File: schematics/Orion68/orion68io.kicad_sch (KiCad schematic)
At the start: 38 parts, among them J1 LevelConverter, J200 Euro96pin, U200 GAL16V8, U25 SN74LVC245APW, U26 SN74LVC245APW, U27 RP5C01A, U30 LM2937xT, Y3 Crystal

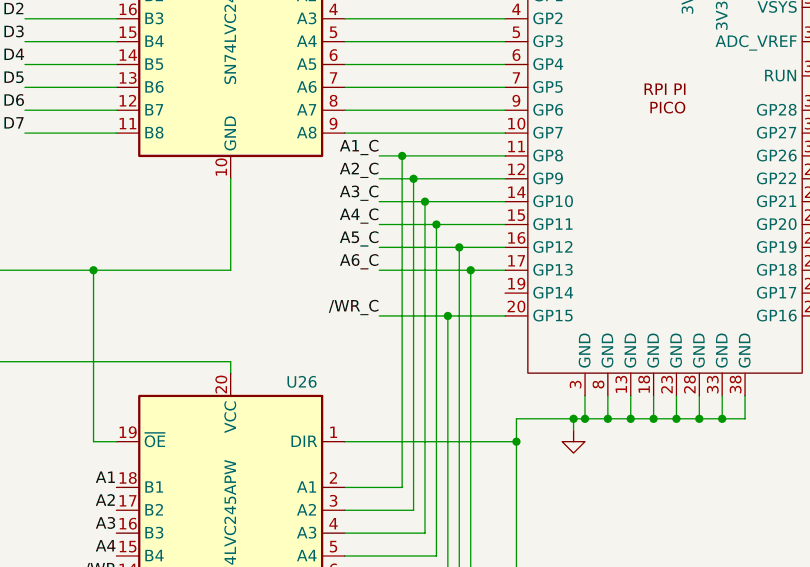
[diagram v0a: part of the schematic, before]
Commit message: Implemented CS_KBD
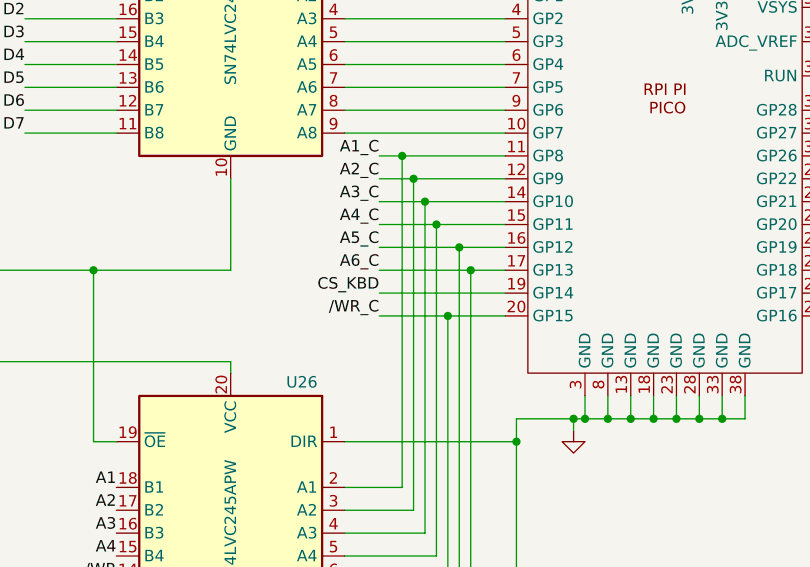
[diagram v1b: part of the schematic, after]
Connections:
- net CS_KBD: now also U_S200.19 (GP14)
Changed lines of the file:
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@@
 	(wire
 		(pts
+			(xy 176.53 143.51) (xy 190.5 143.51)
+		)
+		(stroke
+			(width 0)
+			(type default)
+		)
+	)
+	(wire
+		(pts
 			(xy 176.53 133.35) (xy 181.61 133.35)
 		)
@@
 		)
 	)
+	(label "CS_KBD"
+		(at 176.53 143.51 180)
+		(effects
+			(font
+				(size 1.27 1.27)
+			)
+			(justify right bottom)
+		)
+	)

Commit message: Changed dtack system
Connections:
- net RX_OUT is gone; now on net CS_KBD: J1.9 (Pin_9)
- net CS_KBD: no longer U_S200.19 (GP14)
- net /CS_MULTIO: now also J200.60
- net /DTACK_MIO: now reaches J200.61
- net /DTACK_MIO: now also U_S200.19 (GP14)
- net RX renamed CS_KBD_C
- net TX: no longer names the net of J1.4 (Pin_4)
- net TX_OUT: no longer names the net of J1.3 (Pin_3)
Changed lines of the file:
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@@
 	(wire
 		(pts
+			(xy -26.67 137.16) (xy -26.67 114.3)
+		)
+		(stroke
+			(width 0)
+			(type default)
+		)
+	)
+	(wire
+		(pts
 			(xy 270.51 207.01) (xy 270.51 208.28)
 		)
@@
 	(wire
 		(pts
+			(xy -26.67 114.3) (xy -24.13 114.3)
+		)
+		(stroke
+			(width 0)
+			(type default)
+		)
+	)
+	(wire
+		(pts
 			(xy -10.16 116.84) (xy -13.97 116.84)
 		)
@@
 	(wire
 		(pts
+			(xy -29.21 134.62) (xy -29.21 116.84)
+		)
+		(stroke
+			(width 0)
+			(type default)
+		)
+	)
+	(wire
+		(pts
 			(xy -12.7 50.8) (xy -13.97 50.8)
 		)
@@
 	(wire
 		(pts
+			(xy -31.75 137.16) (xy -26.67 137.16)
+		)
+		(stroke
+			(width 0)
+			(type default)
+		)
+	)
+	(wire
+		(pts
 			(xy -34.29 119.38) (xy -35.56 119.38)
 		)
@@
 	(wire
 		(pts
+			(xy -29.21 116.84) (xy -24.13 116.84)
+		)
+		(stroke
+			(width 0)
+			(type default)
+		)
+	)
+	(wire
+		(pts
 			(xy 172.72 113.03) (xy 190.5 113.03)
 		)
@@
 	(wire
 		(pts
+			(xy -31.75 134.62) (xy -29.21 134.62)
+		)
+		(stroke
+			(width 0)
+			(type default)
+		)
+	)
+	(wire
+		(pts
 			(xy 232.41 248.92) (xy 242.57 248.92)
 		)
@@
 		)
 	)
-	(label "TX_OUT"
-		(at 276.86 125.73 0)
-		(effects
-			(font
-				(size 1.27 1.27)
-			)
-			(justify left bottom)
-		)
-	)
 	(label "D3"
 		(at -34.29 55.88 0)
@@
 		)
 	)
-	(label "RX"
-		(at 264.16 133.35 180)
-		(effects
-			(font
-				(size 1.27 1.27)
-			)
-			(justify right bottom)
-		)
-	)
 	(label "5V"
 		(at 276.86 130.81 0)
@@
 		)
 	)
+	(label "CS_KBD"
+		(at 276.86 133.35 0)
+		(effects
+			(font
+				(size 1.27 1.27)
+			)
+			(justify left bottom)
+		)
+	)
 	(label "{slash}iowr"
 		(at -12.7 71.12 0)
@@
 		)
 	)
+	(label "{slash}CS_MULTIO"
+		(at -31.75 137.16 180)
+		(effects
+			(font
+				(size 1.27 1.27)
+			)
+			(justify right bottom)
+		)
+	)
 	(label "A4"
 		(at 147.32 172.72 180)
@@
 		)
 	)
+	(label "{slash}DTACK_MIO"
+		(at -31.75 134.62 180)
+		(effects
+			(font
+				(size 1.27 1.27)
+			)
+			(justify right bottom)
+		)
+	)
 	(label "+12V"
 		(at -6.35 121.92 0)
@@
 		)
 	)
-	(label "RX_OUT"
-		(at 276.86 133.35 0)
-		(effects
-			(font
-				(size 1.27 1.27)
-			)
-			(justify left bottom)
-		)
-	)
 	(label "D1"
 		(at 137.16 110.49 180)
@@
 		)
 	)
-	(label "CS_KBD"
+	(label "{slash}DTACK_MIO"
 		(at 176.53 143.51 180)
 		(effects
@@
 		)
 	)
-	(label "TX"
-		(at 264.16 125.73 180)
-		(effects
-			(font
-				(size 1.27 1.27)
-			)
-			(justify right bottom)
-		)
-	)
 	(label "A5"
 		(at -34.29 101.6 0)
@@
 		)
 	)
+	(label "CS_KBD_C"
+		(at 264.16 133.35 180)
+		(effects
+			(font
+				(size 1.27 1.27)
+			)
+			(justify right bottom)
+		)
+	)

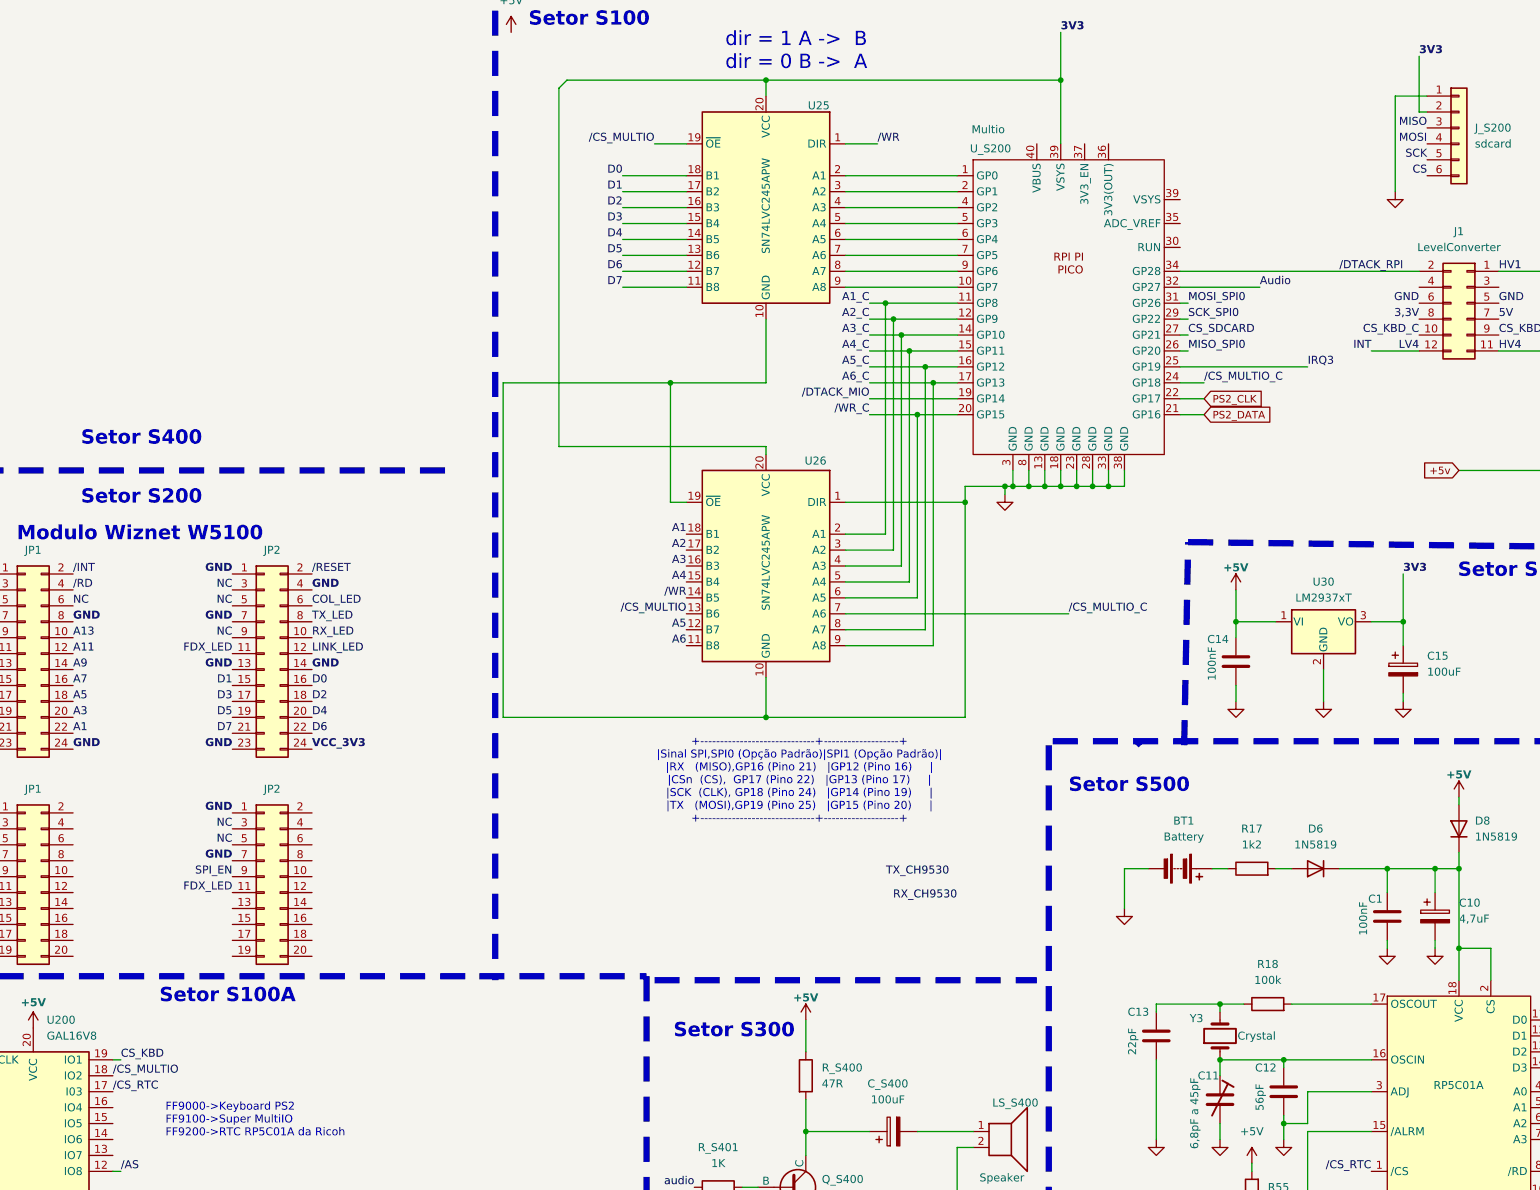
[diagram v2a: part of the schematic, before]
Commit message: SDcard running ok with pico MultiIO
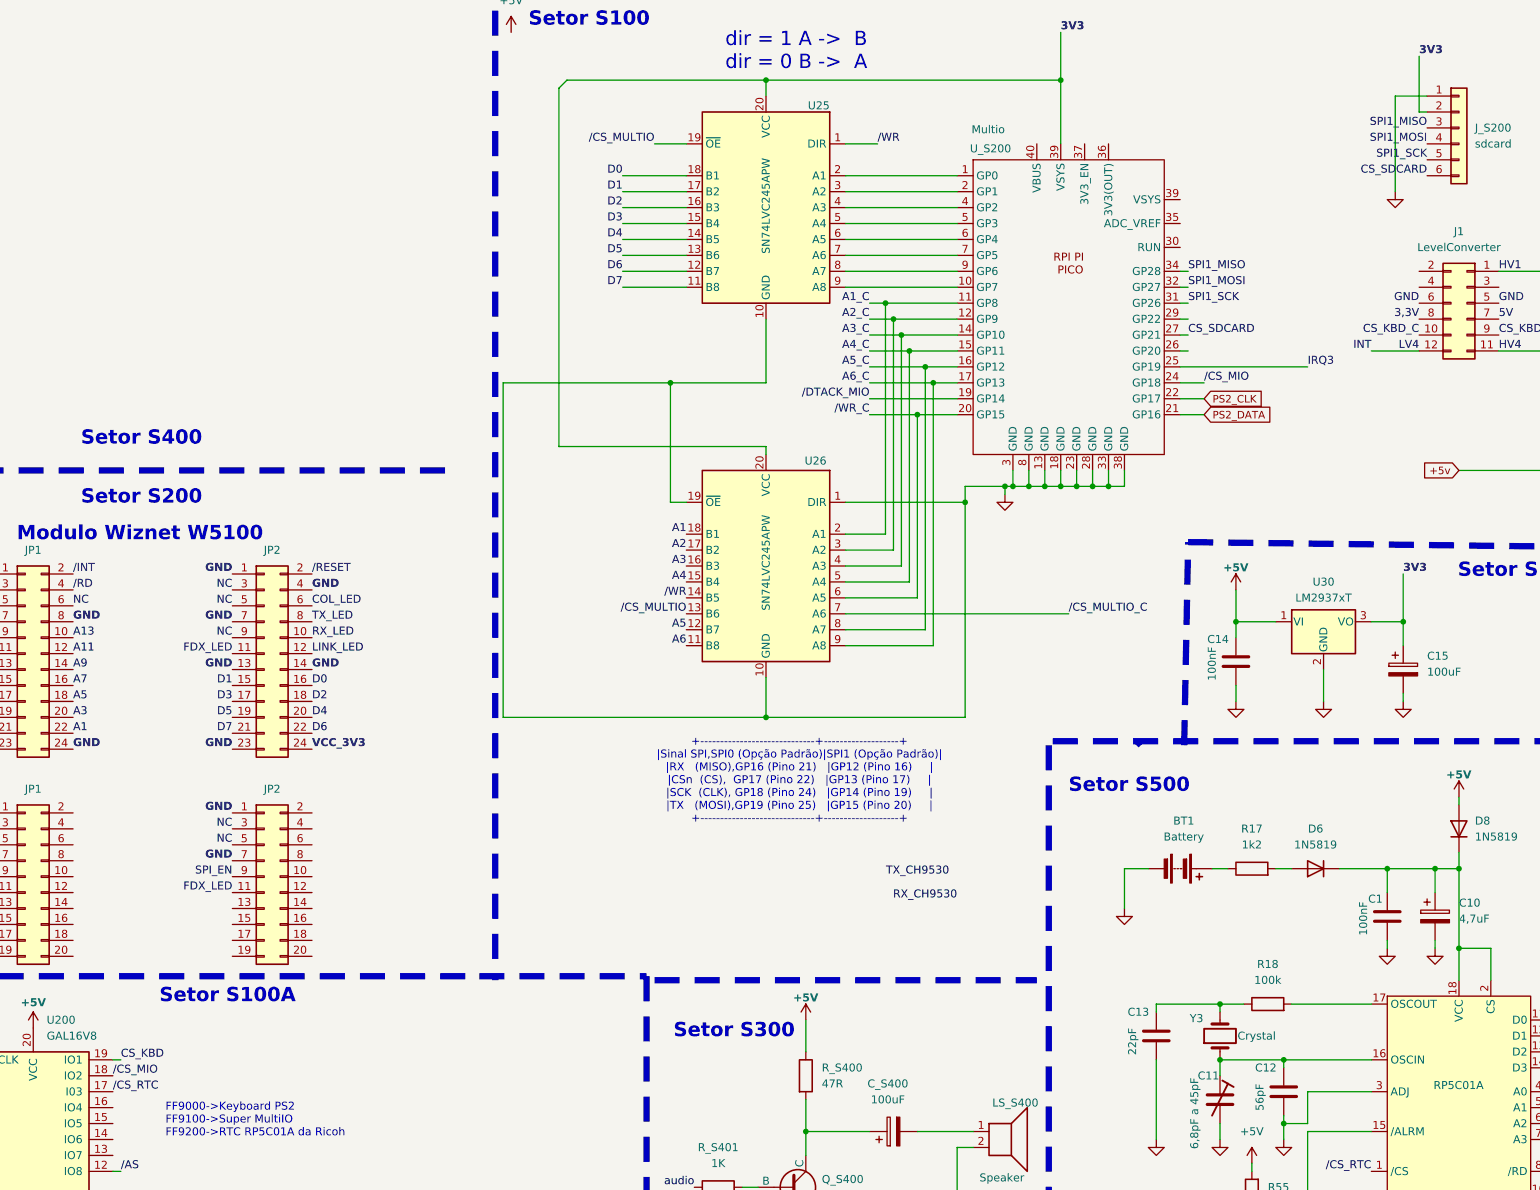
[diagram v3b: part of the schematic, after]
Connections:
- net CS is gone; now on net CS_SDCARD: J_S200.6 (Pin_6)
- net MOSI is gone; now on net SPI1_MOSI: J_S200.4 (Pin_4)
- net SCK is gone; now on net SPI1_SCK: J_S200.5 (Pin_5)
- net /CS_MULTIO: no longer U200.18 (IO2)
- net /CS_MULTIO_C: no longer U_S200.24 (GP18)
- net Audio renamed SPI1_MOSI
- net MISO renamed SPI1_MISO
- net SPI1_MISO: now also U_S200.34 (GP28)
- net MISO_SPI0: no longer names the net of U_S200.26 (GP20)
- net MOSI_SPI0 renamed SPI1_SCK
- net SCK_SPI0: no longer names the net of U_S200.29 (GP22)
- net /DTACK_RPI: no longer names the net of J1.2 (Pin_2)
- net /DTACK_RPI: no longer U_S200.34 (GP28)
- new net /CS_MIO: U200.18 (IO2), U_S200.24 (GP18)
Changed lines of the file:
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@@
 	(wire
 		(pts
+			(xy 227.33 123.19) (xy 226.06 123.19)
+		)
+		(stroke
+			(width 0)
+			(type default)
+		)
+	)
+	(wire
+		(pts
 			(xy 232.41 261.62) (xy 232.41 259.08)
 		)
@@
 	(wire
 		(pts
-			(xy 226.06 123.19) (xy 264.16 123.19)
-		)
-		(stroke
-			(width 0)
-			(type default)
-		)
-	)
-	(wire
-		(pts
 			(xy -29.21 134.62) (xy -29.21 116.84)
 		)
@@
 	(wire
 		(pts
+			(xy 227.33 125.73) (xy 226.06 125.73)
+		)
+		(stroke
+			(width 0)
+			(type default)
+		)
+	)
+	(wire
+		(pts
 			(xy -6.35 121.92) (xy -13.97 121.92)
 		)
@@
 	(wire
 		(pts
-			(xy 238.76 125.73) (xy 226.06 125.73)
-		)
-		(stroke
-			(width 0)
-			(type default)
-		)
-	)
-	(wire
-		(pts
 			(xy 242.57 261.62) (xy 242.57 259.08)
 		)
@@
 		)
 	)
-	(label "CS"
-		(at 265.43 107.95 180)
-		(effects
-			(font
-				(size 1.27 1.27)
-			)
-			(justify right bottom)
-		)
-	)
-	(label "{slash}CS_MULTIO_C"
-		(at 229.87 140.97 0)
-		(effects
-			(font
-				(size 1.27 1.27)
-			)
-			(justify left bottom)
-		)
-	)
 	(label "A7"
 		(at 49.53 189.23 0)
@@
 		)
 	)
-	(label "SCK_SPI0"
-		(at 227.33 130.81 0)
+	(label "SPI1_MOSI"
+		(at 227.33 125.73 0)
 		(effects
 			(font
@@
 		)
 	)
-	(label "MOSI_SPI0"
+	(label "SPI1_SCK"
 		(at 227.33 128.27 0)
 		(effects
@@
 		)
 	)
-	(label "MISO_SPI0"
-		(at 227.33 135.89 0)
+	(label "SPI1_MISO"
+		(at 227.33 123.19 0)
 		(effects
 			(font
@@
 		)
 	)
+	(label "CS_SDCARD"
+		(at 265.43 107.95 180)
+		(effects
+			(font
+				(size 1.27 1.27)
+			)
+			(justify right bottom)
+		)
+	)
 	(label "GND"
 		(at 74.93 171.45 180)
@@
 		)
 	)
-	(label "MOSI"
+	(label "SPI1_MOSI"
 		(at 265.43 102.87 180)
 		(effects
@@
 		)
 	)
-	(label "SCK"
+	(label "SPI1_SCK"
 		(at 265.43 105.41 180)
 		(effects
@@
 		)
 	)
-	(label "{slash}CS_MULTIO"
+	(label "{slash}CS_MIO"
 		(at 55.88 251.46 0)
 		(effects
@@
 		)
 	)
+	(label "{slash}CS_MIO"
+		(at 229.87 140.97 0)
+		(effects
+			(font
+				(size 1.27 1.27)
+			)
+			(justify left bottom)
+		)
+	)
 	(label "{slash}DTACK_MIO"
 		(at 176.53 143.51 180)
@@
 		)
 	)
-	(label "MISO"
+	(label "SPI1_MISO"
 		(at 265.43 100.33 180)
 		(effects
@@
 		)
 	)
-	(label "Audio"
-		(at 238.76 125.73 0)
-		(effects
-			(font
-				(size 1.27 1.27)
-			)
-			(justify left bottom)
-		)
-	)
 	(label "BD15"
 		(at 466.09 187.96 180)
@@
 			)
 			(justify right bottom)
-		)
-	)
-	(label "{slash}DTACK_RPI"
-		(at 261.62 123.19 180)
-		(effects
-			(font
-				(size 1.27 1.27)
-			)
-			(justify right bottom)

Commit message: Implemented new picoVGA V2
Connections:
- net /CS_MULTIO: no longer J200.60
- net /DTACK_MIO: no longer J200.61
- net PRETO: now reaches J200.57
- net VERMELHO: now reaches J200.58
- net /DTACK_PVGA: now reaches J200.59
- net VERDE: now reaches J200.62
- net LILAS: now reaches J200.63
- new net AMARELO: J200.61
- new net MARRON: J200.60
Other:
- note added: "LILAS"

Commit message: Implementede 68681, led blink,uart to test
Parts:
- removed JP1, JP2: Conn_02x10_Odd_Even, symbol Connector_Generic:Conn_02x10_Odd_Even
- removed JP1, JP2: Conn_02x12_Odd_Even, symbol Connector_Generic:Conn_02x12_Odd_Even
- added C18, C19: 7pF, Capacitor_SMD:C_0603_1608Metric, symbol Device:C
- added IC4: XR68C681CJTR-F, Package_LCC:PLCC-44_THT-Socket, symbol rosco_m68k-rescue:XR68C681CJTR-F-XR68C681
- added J22: Kbd_usb, symbol Connector_Generic:Conn_01x05
- added J23: Conn_01x06, rosco_m68k:1X06, symbol Connector_Generic:Conn_01x06
- added LED1: GREEN, rosco_m68k:LED5MM, symbol rosco_m68k-eagle-import:LED5MM
- added LED2: RED, rosco_m68k:LED5MM, symbol rosco_m68k-eagle-import:LED5MM
- added PS/2: Mouse, JJ65c02:mini_din-6, symbol Connector:Mini-DIN-6
- added Q4: 14.7456MHz, Crystal:Crystal_HC49-4H_Vertical, symbol Device:Crystal
- added R56, R57: 1K, Resistor_SMD:R_0603_1608Metric, symbol rosco_m68k-eagle-import:R-EU_0207_10
- added R_S3, R_S4: 4k7, Resistor_THT:R_Axial_DIN0204_L3.6mm_D1.6mm_P5.08mm_Horizontal, symbol Device:R
- added U33: 68681, symbol Interface:68681
- PS/1: value Mini-DIN-6 -> Keyboard
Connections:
- net +5V: now also J22.1 (Pin_1)
- net +5v: now also PS/2.4
- net 3V3: now also R_S3.2, R_S4.2
- net A1: now also IC4.2 (A1), U33.1 (A1)
- net A2: now also IC4.4 (A2), U33.3 (A2)
- net A3: now also IC4.6 (A3), U33.5 (A3)
- net A4: now also IC4.7 (A4), U33.6 (A4)
- net CS_KBD: no longer U200.19 (IO1)
- net D0: now also IC4.28 (D0), U33.25 (D0)
- net D1: now also IC4.18 (D1), U33.16 (D1)
- net D2: now also IC4.27 (D2), U33.24 (D2)
- net D3: now also IC4.19 (D3), U33.17 (D3)
- net D4: now also IC4.26 (D4), U33.23 (D4)
- net D5: now also IC4.20 (D5), U33.18 (D5)
- net D6: now also IC4.25 (D6), U33.22 (D6)
- net D7: now also IC4.21 (D7), U33.19 (D7)
- net GND: now also C18.1, C19.1, IC4.22 (GND), IC4.3 (IP3), IC4.42 (IP5), IC4.43 (IP4), J22.5 (Pin_5), J23.6 (Pin_6), PS/2.3, U33.20 (GND)
- net IRQ4: now also U33.21 (IRQ)
- net RESET: now also IC4.38 (*RESET)
- net /RESET: now also U33.34 (RESET)
- net /WR: no longer U25.1 (DIR), U26.14 (B5)
- net /WR_C: now also U25.1 (DIR)
- net /memwr: now also U26.14 (B5), U33.8 (R/W)
- new net: IC4.15 (OP3), LED2.K (C)
- new net: IC4.16 (OP5), LED1.K (C)
- new net: LED1.A, R56.1
- new net: LED2.A, R57.1
- new net: C19.2, Q4.2, U33.33 (X2)
- new net: C18.2, Q4.1, U33.32 (X1/CLK)
- new net CTSA: IC4.8 (IP0)
- new net CTSB: IC4.5 (IP1)
- new net DTACK: IC4.10 (*DTALK)
- new net DUAIACK: IC4.41 (*IACK)
- new net DUAIRQ: IC4.24 (INTR)
- new net DUASEL: IC4.39 (CS)
- new net PS2_CLK1: PS/2.5, R_S3.1
- new net PS2_DATA1: PS/2.1, R_S4.1
- new net RTSA: IC4.32 (OP0)
- new net RTSB: IC4.14 (OP1)
- new net RW: IC4.9 (*R/*W)
- new net RXDA: IC4.35 (RXDA), J22.3 (Pin_3), U33.31 (RXDA)
- new net RXDB: IC4.11 (RXDB)
- new net SPICLK: IC4.30 (OP4), J23.2 (Pin_2), U33.27 (OP4)
- new net SPICS: IC4.31 (OP2), J23.1 (Pin_1), U33.28 (OP2)
- new net SPICS2: IC4.17 (OP7), U33.15 (OP7)
- new net SPIMISO: IC4.40 (IP2), J23.4 (Pin_4), U33.36 (IP2)
- new net SPIMOSI: IC4.29 (OP6), J23.3 (Pin_3), U33.26 (OP6)
- new net TXDA: IC4.33 (TXDA), J22.4 (Pin_4), U33.30 (TXDA)
- new net TXDB: IC4.13 (TXDB)
- new net VCC: IC4.44 (VCC), J23.5 (Pin_5), R56.2, R57.2
- new net /CS_DUART: U200.19 (IO1), U33.35 (CS)
- new net /DT_DUART: U33.9 (DTACK)
- no-connect marks 8 -> 10
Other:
- note added: "CS"
- note added: "FF9000->DUART -Uart1 = Keyboard USB Uart2=livre FF9100->Super MultiIO FF9200->RTC RP5C01A da Ricoh"
- note added: "MISO"
- note added: "MOSI"
- note added: "SCK"
- note removed: "FF9000->Keyboard PS2 FF9100->Super MultiIO FF9200->RTC RP5C01A da Ricoh"
- note removed: "Modulo Wiznet W5100"
- moved on the sheet: J1, J200, J_S200, R_S1, R_S2
